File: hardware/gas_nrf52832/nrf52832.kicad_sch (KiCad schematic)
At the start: 19 parts, among them J1 J-link, J4 Conn_01x03, Q2 FDV303N, Q3 FDV303N, X1 32.768kHz

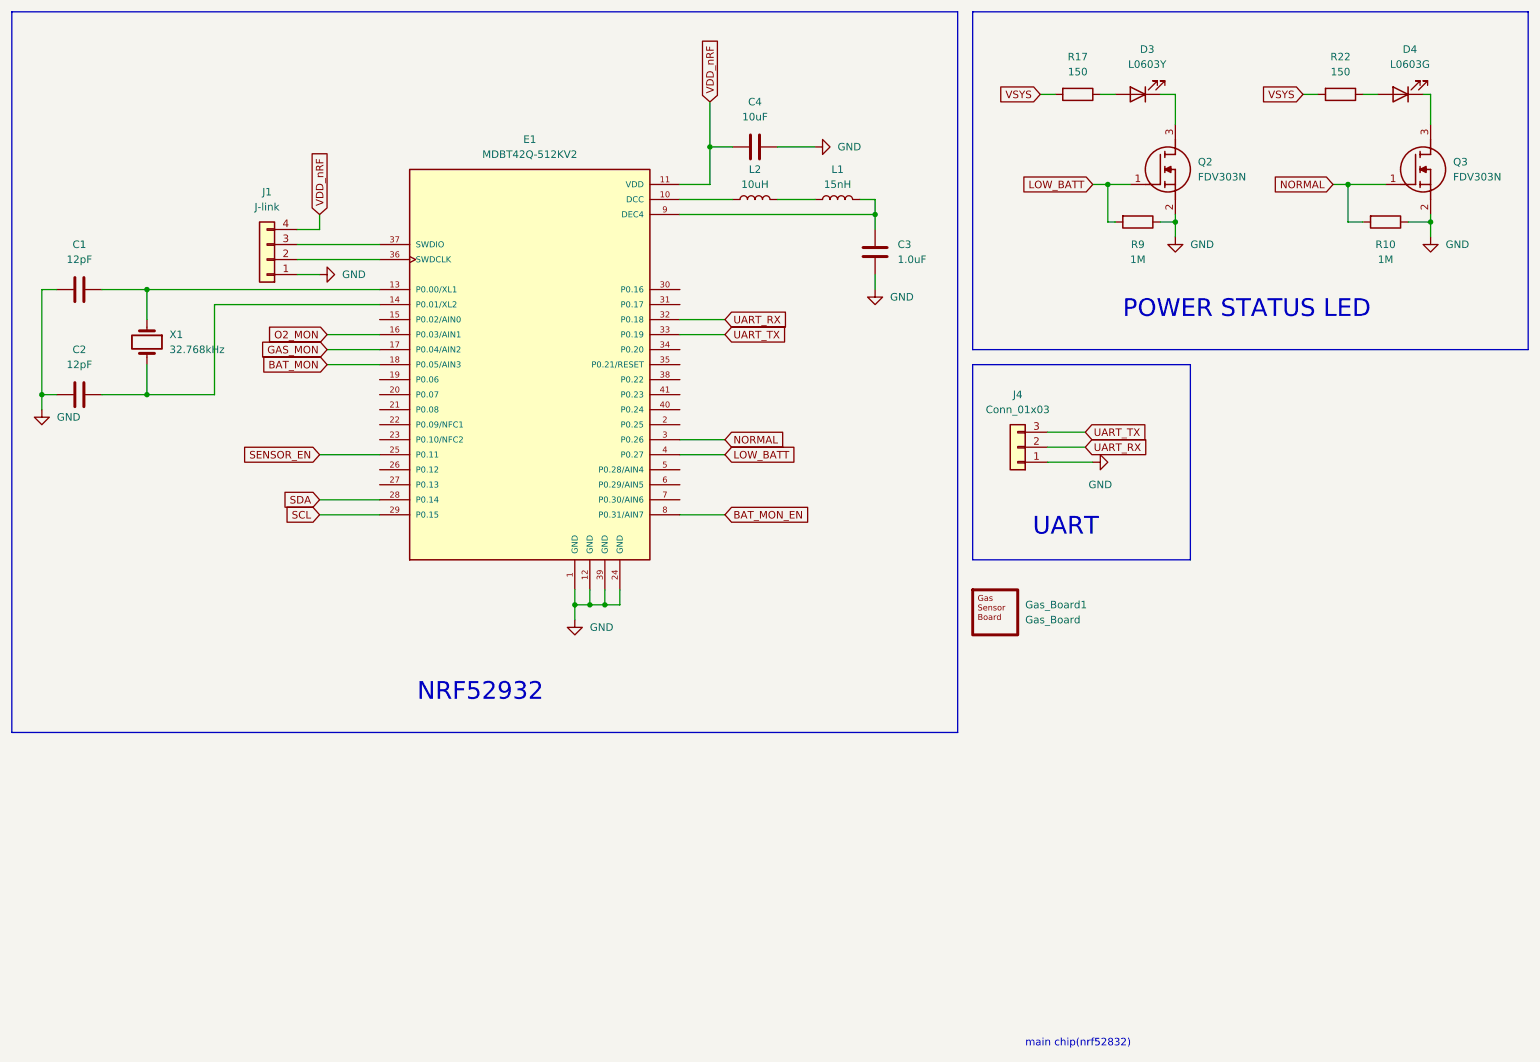
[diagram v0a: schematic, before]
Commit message: hw: fix sensor circuit & fix ERC Error
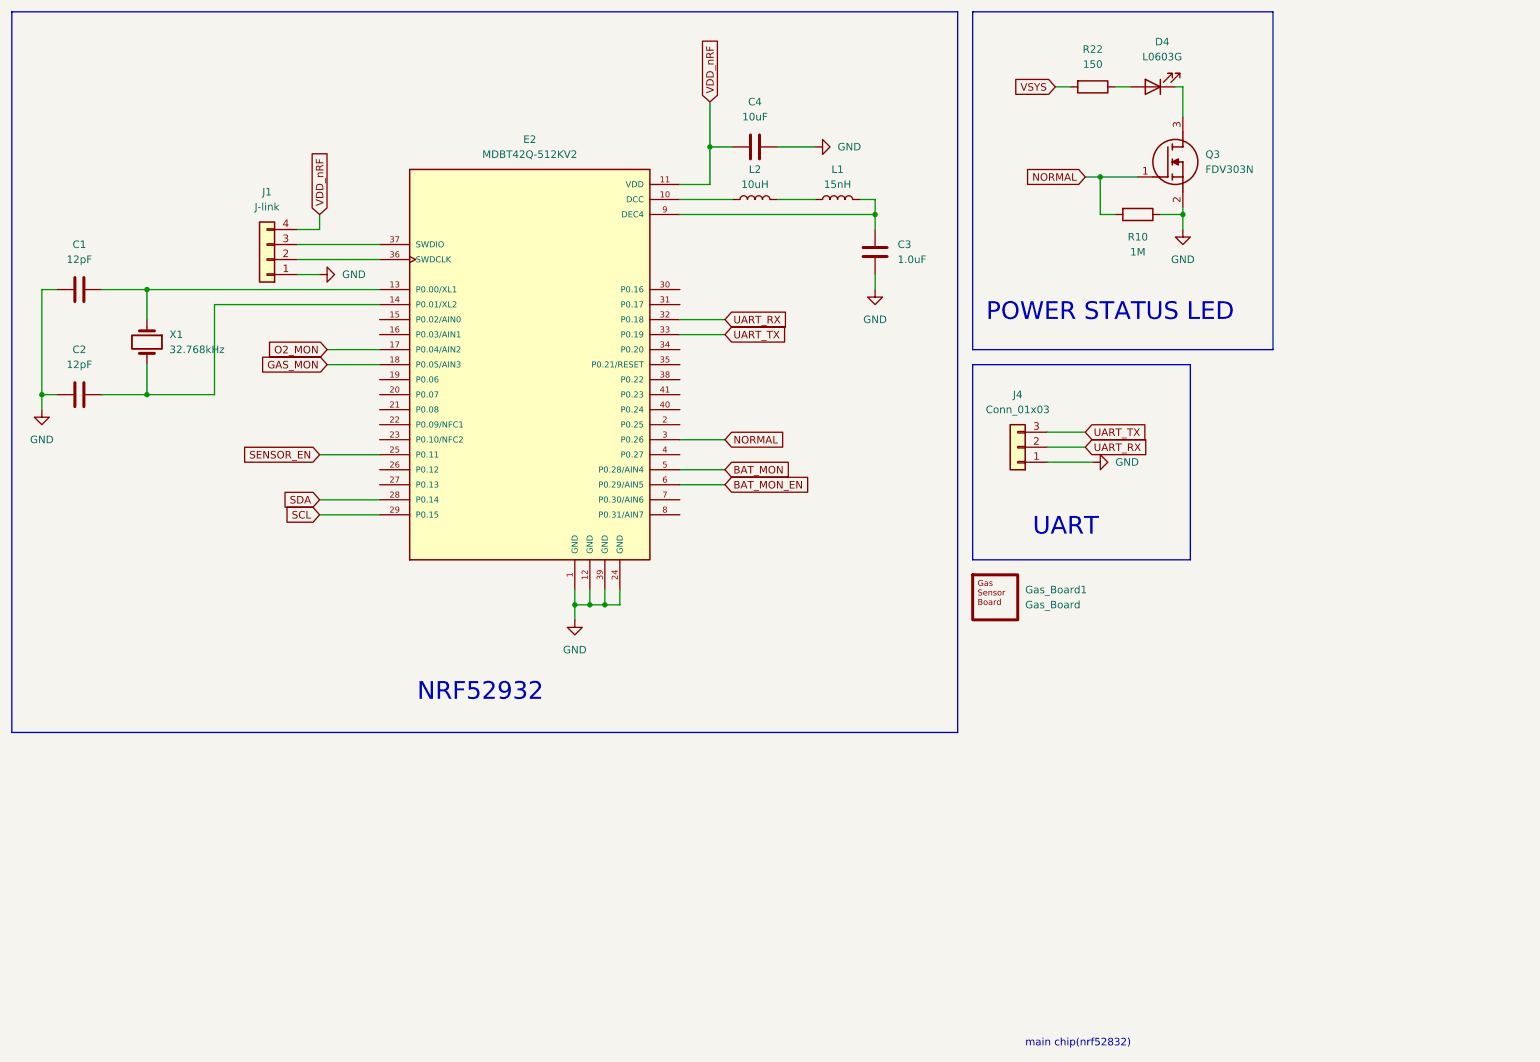
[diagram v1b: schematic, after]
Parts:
- removed D3: L0603Y, LED_SMD:LED_0603_1608Metric, symbol Device:LED
- removed E1: MDBT42Q-512KV2, MDBT42Q-512KV2:RAYTAC_MDBT42Q-512KV2, symbol MDBT42Q-512KV2:MDBT42Q-512KV2
- removed Gas_Board1: Gas_Board, HHS:gas_nordic_edge, symbol DFRobot:Gas_Board
- removed Q2: FDV303N, FDV303N:SOT96P237X111-3N, symbol FDV303N:FDV303N
- removed R17: 150, Resistor_SMD:R_0402_1005Metric, symbol Device:R
- removed R9: 1M, Resistor_SMD:R_0402_1005Metric, symbol Device:R
- added E2: MDBT42Q-512KV2, MDBT42Q-512KV2:RAYTAC_MDBT42Q-512KV2, symbol MDBT42Q-512KV2:MDBT42Q-512KV2
- added Gas_Board1: Gas_Board, HHS:gas_nordic_edge, symbol gas_board:Gas_Board
- C3, C4: footprint Capacitor_SMD:C_0603_1608Metric -> Capacitor_SMD:C_0402_1005Metric
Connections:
- net BAT_MON: now also E2.5 (P0.28/AIN4)
- net BAT_MON_EN: now also E2.6 (P0.29/AIN5)
- net GAS_MON: now also E2.18 (P0.05/AIN3)
- net GND: now also E2.1 (GND), E2.12 (GND), E2.24 (GND), E2.39 (GND)
- net NORMAL: now also E2.3 (P0.26)
- net O2_MON: now also E2.17 (P0.04/AIN2)
- net SCL: now also E2.29 (P0.15)
- net SDA: now also E2.28 (P0.14)
- net SENSOR_EN: now also E2.25 (P0.11)
- net UART_RX: now also E2.32 (P0.18)
- net UART_TX: now also E2.33 (P0.19)
- net VDD_nRF: now also E2.11 (VDD)
- net at L2.1: now also E2.10 (DCC)
- net at C1.2, X1.1: now also E2.13 (P0.00/XL1)
- net at C2.2, X1.2: now also E2.14 (P0.01/XL2)
- net at J1.2 (Pin_2): now also E2.36 (SWDCLK)
- net at J1.3 (Pin_3): now also E2.37 (SWDIO)
- net at C3.1, L1.2: now also E2.9 (DEC4)
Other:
- moved on the sheet: D4, R10, R22

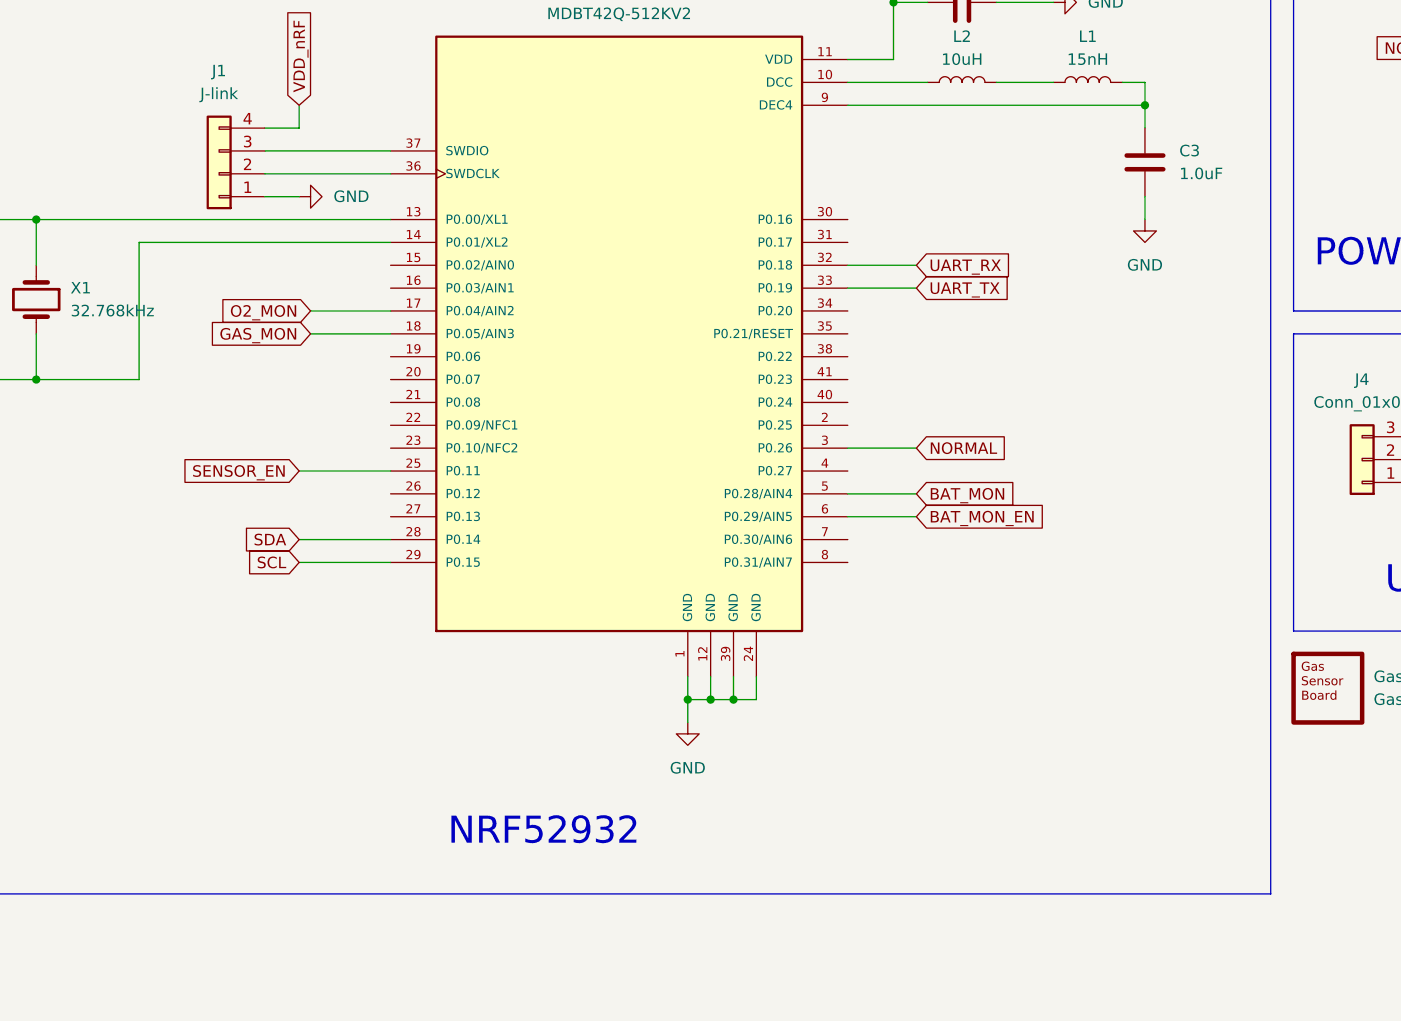
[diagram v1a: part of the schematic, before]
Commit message: feat: hw revision 1.0.2
Rev 1.0.2
- Oxygen Sensor
	- Voltage Amplification Ratio AdjustmentR18(10.7 -> 10k), R12(2.0k -> 2M)
	-> Reduce Current Consumption
	- Addition of lowpass filter for Noise Reduction
- Gas Sensor
	- Addition of lowpass filter for Noise Reduction
- 2 Layter -> 4 Layer
- hansam digitec requirement
	- If USB and RC are very close, errors may occur
	so increase the distance (R1, R23, R24, C22)
- BME680 Sensor Enable ctrl remove
- 32k Crystal Layout fix
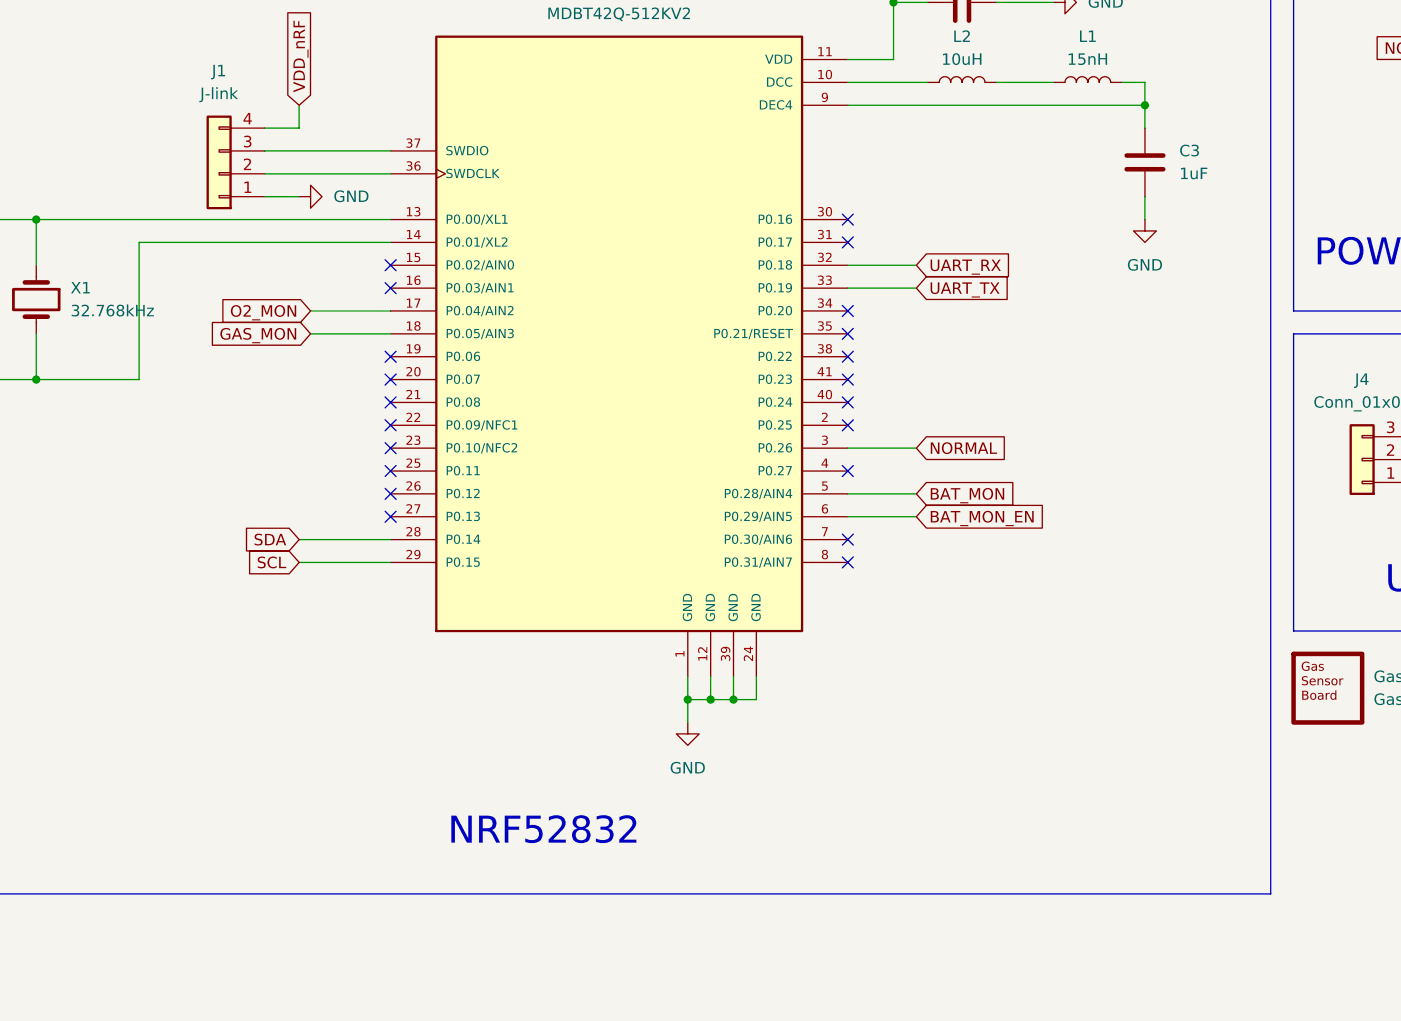
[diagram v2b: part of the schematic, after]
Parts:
- C1, C2: MANUFACTURER (none) -> Samsung Electro-Mechanics; Manufacturer_Part_Number (none) -> CL05C120JB5NNNC; Package (none) -> 0402 (1005 Metric); Type (none) -> Surface Mount
- C3: value 1.0uF -> 1uF; MANUFACTURER (none) -> Murata Electronics; Manufacturer_Part_Number (none) -> GRM155C71A105ME11D; Package (none) -> 0402 (1005 Metric); Type (none) -> Surface Mount
- C4: MANUFACTURER (none) -> Murata Electronics; Manufacturer_Part_Number (none) -> GRM155C80J106ME11D; Package (none) -> 0402 (1005 Metric); Type (none) -> Surface Mount
- D4: MANUFACTURER (none) -> BRIGHT LED; Manufacturer_Part_Number (none) -> BL-HG036A-AV-TRB; Package (none) -> 0603 (1608 Metric); Type (none) -> Surface Mount
- E2: Manufacturer_Part_Number (none) -> MDBT42Q-512KV2; Package SMD-41 Raytac Corporation -> SMD-41; Type (none) -> Surface Mount
- Gas_Board1: now left out of the parts list
- L1: MANUFACTURER (none) -> TDK; Manufacturer_Part_Number (none) -> MLG1005S15NJT000; Package (none) -> 0402 (1005 Metric); Type (none) -> Surface Mount
- L2: MANUFACTURER (none) -> Murata Electronics; Manufacturer_Part_Number (none) -> LQM18FN100M00D; Package (none) -> 0603 (1608 Metric); Type (none) -> Surface Mount
- Q3: MANUFACTURER (none) -> ONSEMI; Package (none) -> SOT-23; Type (none) -> Surface Mount
- R10: MANUFACTURER (none) -> YAGEO; Manufacturer_Part_Number (none) -> RC0402FR-071ML; Package (none) -> 0402 (1005 Metric); Type (none) -> Surface Mount
- R22: MANUFACTURER (none) -> TA-I Tech; Manufacturer_Part_Number (none) -> RM04FTN1500; Package (none) -> 0402 (1005 Metric); Type (none) -> Surface Mount
- X1: MANUFACTURER (none) -> EPSON; Manufacturer_Part_Number (none) -> FC-135 32.7680KA-A5; Package (none) -> SMD3215-2P; Type (none) -> Surface Mount
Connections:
- net SENSOR_EN: no longer names the net of E2.25 (P0.11)
- no-connect marks 0 -> 21
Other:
- note added: "NRF52832"
- note removed: "NRF52932"
